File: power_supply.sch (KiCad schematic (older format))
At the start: 62 parts, among them J1 12v, 0.5A nominal, 5A Surge, J2 5V 25W, J3 Fan, J4 Program, J5 Shutdown, J6 12V 5V, J7 Serial Debug, J8 REMOVE to PRGM, J9 Main PWR SW, M1 U3V70F5, M2 XL4015, M3 U1V11F5, Q1 BSS806, Q2 BSS806, Q3 SI2369BDS, Q4 BSS806, Q5 IRF9540NPBF, U1 ALD910027, U2 MCP9700A, U3 BTS443P, U4 PIC16F1709, U5 MCP111-195

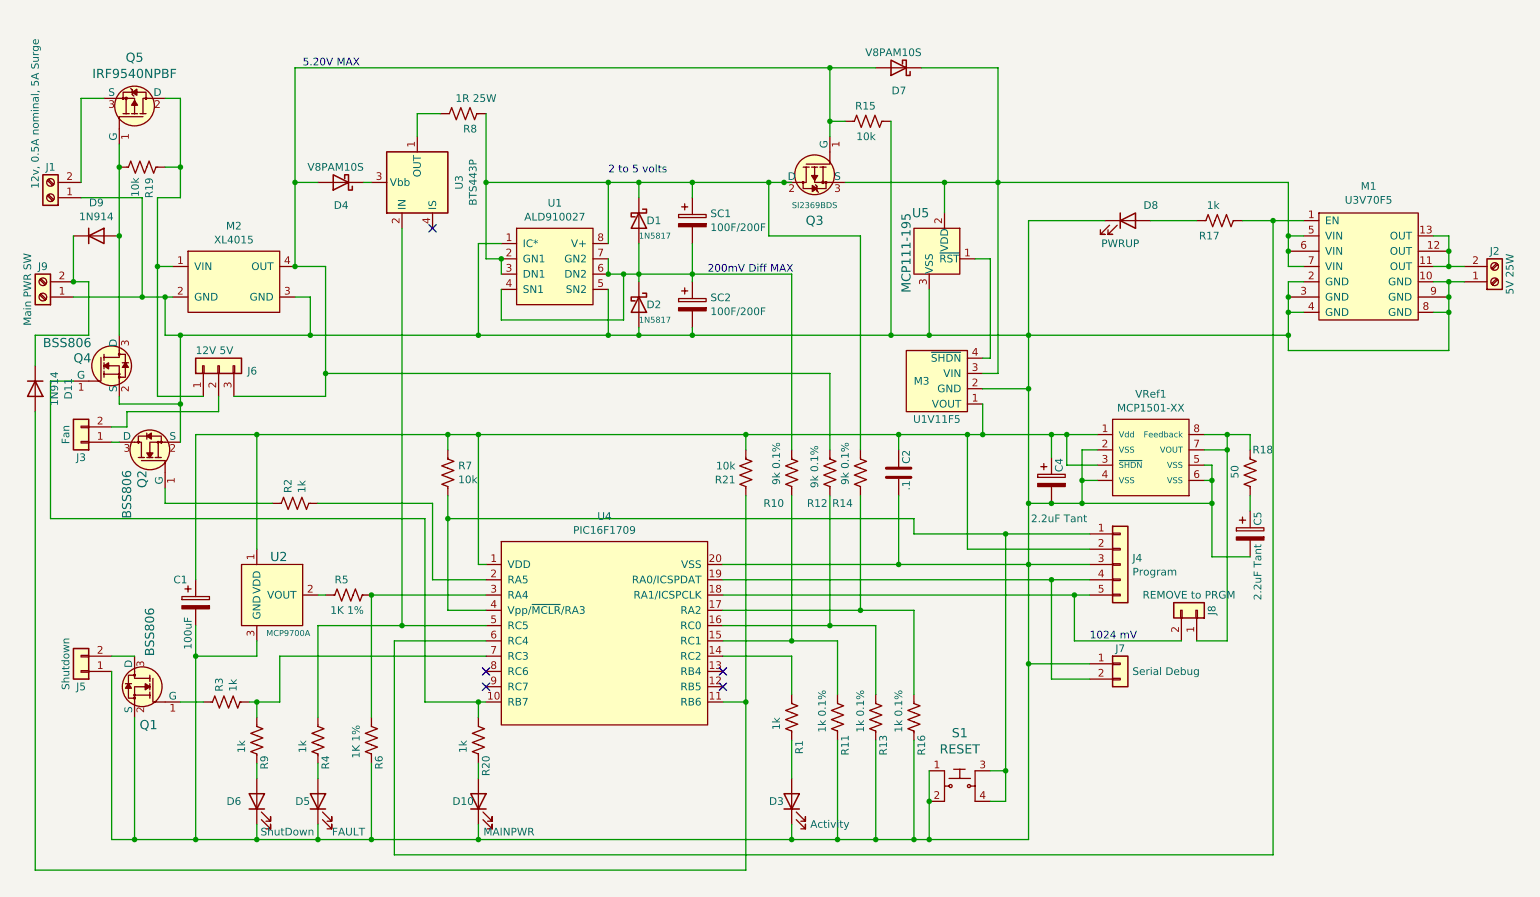
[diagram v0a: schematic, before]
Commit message: Version 0.35 includes updates for new parts and field updates for PCB
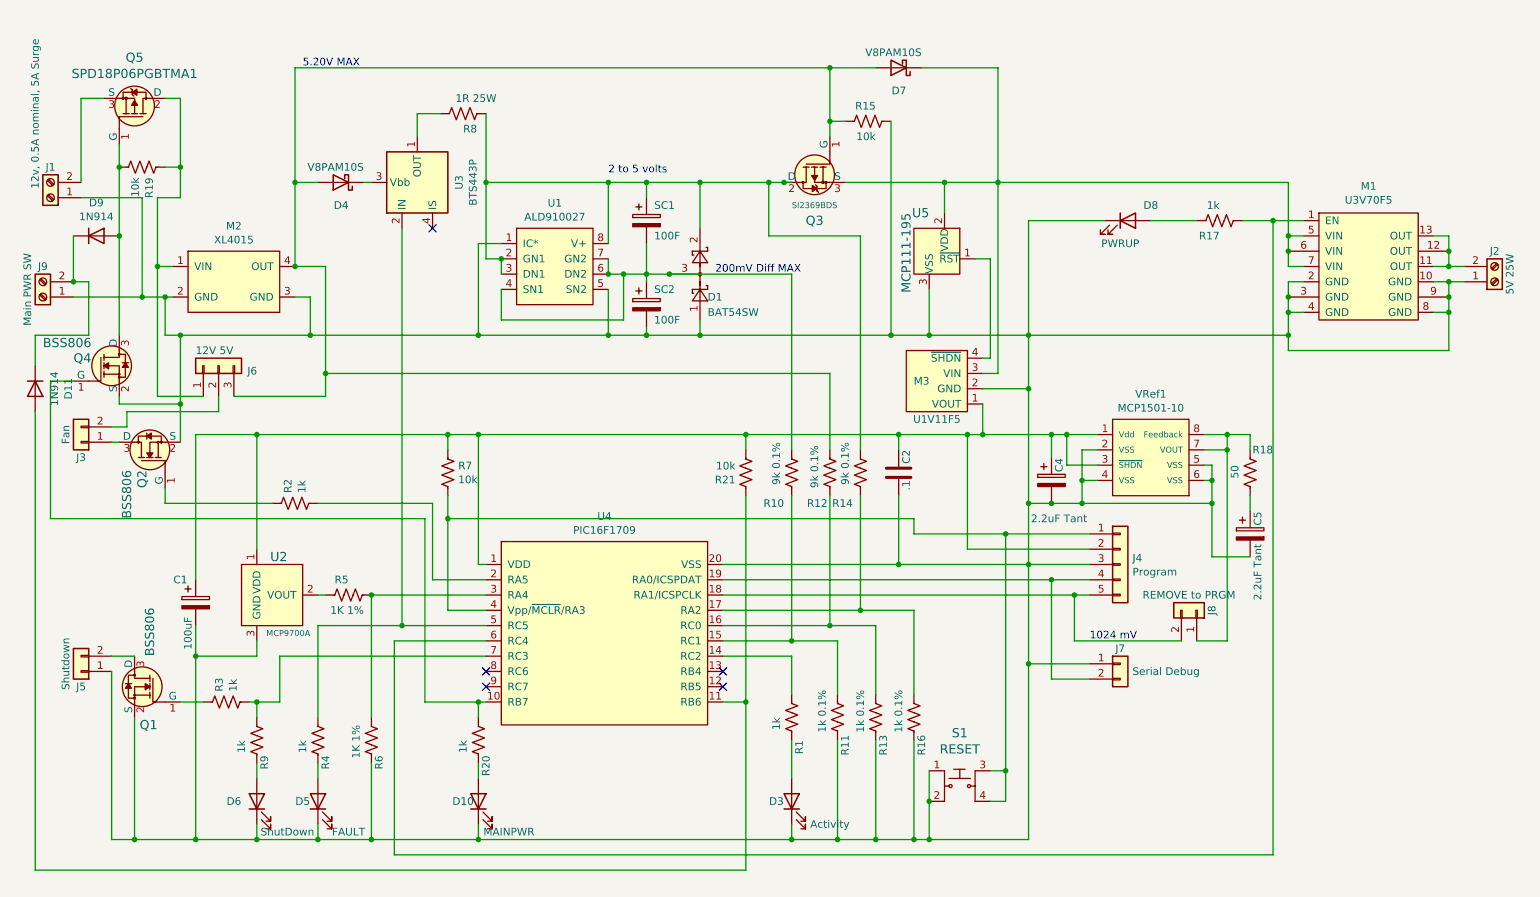
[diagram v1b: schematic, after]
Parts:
- removed D1, D2: 1N5817, Diode_THT:D_DO-41_SOD81_P10.16mm_Horizontal, symbol Diode:1N5817
- added D1: BAT54SW, Package_TO_SOT_SMD:SOT-323_SC-70, symbol Diode:BAT54SW
- C1: footprint (none) -> Capacitor_SMD:CP_Elec_6.3x5.2
- C4, C5: footprint (none) -> Capacitor_Tantalum_SMD:CP_EIA-3216-18_Kemet-A; Part# (none) -> 80-T491A225K010; Vendor (none) -> Mouser
- D4, D7: Part# (none) -> 78-V8PAM10SHM3/H; Vendor (none) -> Mouser
- M2: footprint (none) -> Footprint_Library:XL4015
- M3: footprint (none) -> Pololu:U1V11Fx
- Q1: Category Discrete Semiconductor Products -> (none); DK_Datasheet_Link https://www.onsemi.com/pub/Collateral/BSS138-D.PDF -> (none); DK_Detail_Page /product-detail/en/on-semiconductor/BSS138/BSS138CT-ND/2442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 -> (none); Description MOSFET N-CH 50V 220MA SOT-23 -> (none); Digi-Key_PN BSS138CT-ND -> (none); Family Transistors - FETs, MOSFETs - Single -> (none); MPN BSS138 -> (none); Manufacturer ON Semiconductor -> (none); Part# (none) -> 726-BSS806NEH6327XTS; Status Active -> (none); Vendor (none) -> Mouser
- Q2, Q4: Part# (none) -> 726-BSS806NEH6327XTS; Vendor (none) -> Mouser
- Q5: value IRF9540NPBF -> SPD18P06PGBTMA1; footprint digikey-footprints:TO-220-3 -> Package_TO_SOT_SMD:TO-252-3_TabPin2
- SC1, SC2: value 100F/200F -> 100F
- U1: Part# (none) -> 585-ALD910027SAL; Vendor (none) -> Mouser
- U2: Category Sensors, Transducers -> (none); DK_Datasheet_Link http://www.microchip.com/mymicrochip/filehandler.aspx?ddocn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 -> (none); DK_Detail_Page /product-detail/en/microchip-technology/MCP9700A-E-TO/MCP97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 -> (none); Description SENSOR ANALOG -40C-125C TO92-3 -> (none); Digi-Key_PN MCP9700A-E/TO-ND -> (none); Family Temperature Sensors - Analog and Digital Output -> (none); MPN MCP9700A-E/TO -> (none); Manufacturer Microchip Technology -> (none); Part# (none) -> 579-MCP9700A-E/TO; Status Active -> (none); Vendor (none) -> Mouser
- U4: footprint (none) -> Package_SO:SOIC-20W_7.5x12.8mm_P1.27mm; Part# (none) -> 579-PIC16F1709T-I/SO; Vendor (none) -> Mouser
- VRef1: value MCP1501-XX -> MCP1501-10; footprint (none) -> digikey-footprints:SOT-23-6; Part# (none) -> 579-MCP1501T-10E/CHY
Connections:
- net at C1.2, C2.1, C4.2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: now also D1.1
- net at Q3.2 (D), R14.1, R8.2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: now also D1.2
- net at R10.1, SC1.1, SC2.2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: now also D1.3
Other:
- moved on the sheet: SC1, SC2

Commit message: Version 0.36 circuit part changes, completed initial parts information and BOM
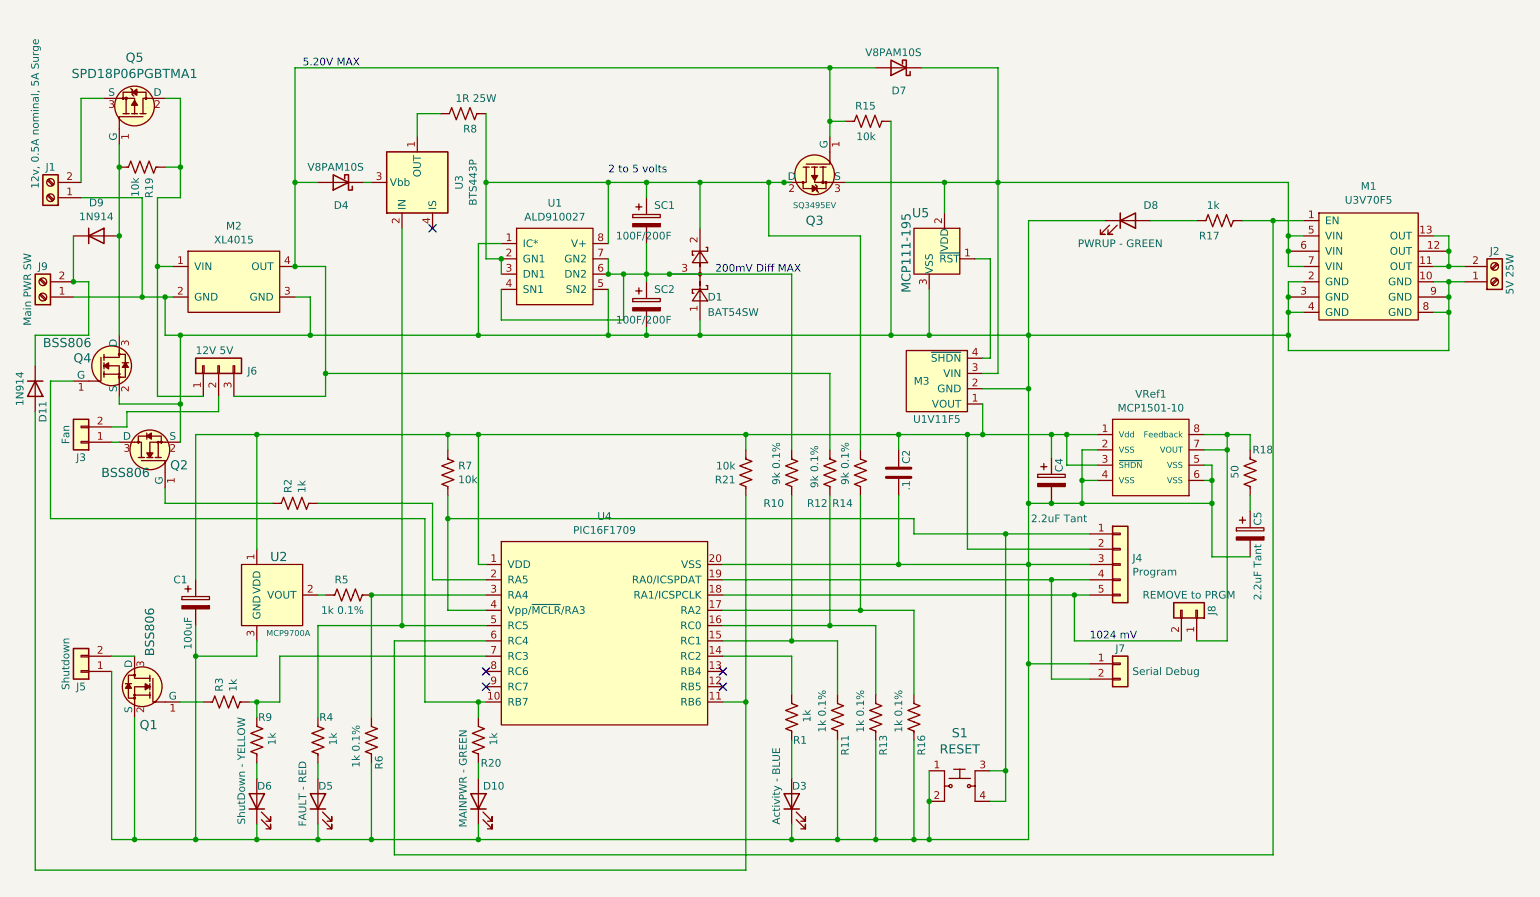
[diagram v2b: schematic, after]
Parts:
- C1: Part# (none) -> 661-EMVY160ADA101MF5; Vendor (none) -> Mouser
- C2: Part# (none) -> 77-VJ1206Y104MXJPBC; Vendor (none) -> Mouser
- D10: value MAINPWR -> MAINPWR - GREEN; Part# (none) -> 645-598-8270-107F; Vendor (none) -> Mouser
- D11, D9: footprint Diode_THT:D_DO-35_SOD27_P7.62mm_Horizontal -> Diode_SMD:D_SOD-123F; Part# (none) -> 821-1N914BWRHG; Vendor (none) -> Mouser
- D3: value Activity -> Activity - BLUE; Part# (none) -> 645-598-8291-107F; Vendor (none) -> Mouser
- D5: value FAULT -> FAULT - RED; Part# (none) -> 645-598-8220-107F; Vendor (none) -> Mouser
- D6: value ShutDown -> ShutDown - YELLOW; Part# (none) -> 645-598-8240-107F; Vendor (none) -> Mouser
- D8: value PWRUP -> PWRUP - GREEN; Part# (none) -> 645-598-8270-107F; Vendor (none) -> Mouser
- J1, J2, J9: Part# (none) -> https://www.amazon.com/Pieces-Pinch-Mount-Terminal-Connecto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; Vendor (none) -> Amazon
- J3, J4, J5, J7, J8: Part# (none) -> https://www.amazon.com/Header-Lystaii-Pin-Connector-Electro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; Vendor (none) -> Amazon
- J6: footprint (none) -> Connector_PinHeader_2.54mm:PinHeader_1x03_P2.54mm_Vertical; Part# (none) -> https://www.amazon.com/Header-Lystaii-Pin-Connector-Electro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; Vendor (none) -> Amazon
- M1: Part# (none) -> 2891; Vendor (none) -> Pololu
- M2: Part# (none) -> https://www.amazon.com/Adjustable-Converter-1-25-36v-Effici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; Vendor (none) -> Amazon
- M3: Part# (none) -> 2562; Vendor (none) -> Pololu
- Q3: value SI2369BDS -> SQ3495EV; footprint digikey-footprints:TO-220-3 -> digikey-footprints:SOT-23-6; Part# (none) -> 78-SQ3495EV-T1_GE3; Vendor (none) -> Mouser
- Q5: Part# (none) -> 726-SPD18P06P; Vendor (none) -> Mouser
- R1, R17, R2, R20, R3, R4, R9: Part# (none) -> 603-RT1206FRD071KL; Vendor (none) -> Mouser
- R10, R12, R14: Part# (none) -> 603-RT1206BRD079KL; Vendor (none) -> Mouser
- R11, R13, R16: Part# (none) -> 603-RT1206BRD071KL; Vendor (none) -> Mouser
- R15, R19, R21, R7: Part# (none) -> 603-RT1206FRD0710KL; Vendor (none) -> Mouser
- R18: Part# (none) -> 660-RN732BTTD50R0B25; Vendor (none) -> Mouser
- R5, R6: value 1K 1% -> 1k 0.1%; Part# (none) -> 603-RT1206BRD071KL; Vendor (none) -> Mouser
- R8: footprint Resistor_SMD:R_1206_3216Metric -> Connector_Wire:SolderWire-0.25sqmm_1x02_P4.5mm_D0.65mm_OD2mm; Part# (none) -> 71-RH0251R000FE02; Vendor (none) -> Mouser
- S1: footprint digikey-footprints:Switch_Tactile_THT_6x6mm -> digikey-footprints:Switch_Tactile_SMD_6x6mm; Part# (none) -> 667-EVQ-7Q201W; Vendor (none) -> Mouser
- SC1, SC2: value 100F -> 100F/200F; Part# (none) -> 581-SCCW45B107SSB / 581-SCCW45B207SSB; Vendor (none) -> Mouser
- U3: Part# (none) -> 726-BTS443P; Vendor (none) -> Mouser
- U5: Part# (none) -> 579-MCP111T-195I/TT; Vendor (none) -> Mouser
- VRef1: Vendor (none) -> Mouser

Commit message: Version 1.0 includes fixes/changes and FRAM support
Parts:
- removed J3: Fan, Connector_PinHeader_2.54mm:PinHeader_1x02_P2.54mm_Vertical, symbol Connector_Generic:Conn_01x02
- removed J9: Main PWR SW, Connectors:Screw_Terminal_2Pin, symbol Connector:Screw_Terminal_01x02
- removed Q3: SQ3495EV, digikey-footprints:SOT-23-6, symbol dk_Transistors-FETs-MOSFETs-Single:IRF9540NPBF
- removed VRef1: MCP1501-10, digikey-footprints:SOT-23-6, symbol Geekgineering:MCP1501-XX
- added C5, C6: 1uF, Capacitor_SMD:C_1206_3216Metric_Pad1.33x1.80mm_HandSolder, symbol Device:CP
- added J2: Power Switch, Connector_JST:JST_XH_B5B-XH-A_1x05_P2.50mm_Vertical, symbol Connector_Generic:Conn_01x05
- added J9: FRAM I2C, Connector_JST:JST_XH_B3B-XH-A_1x03_P2.50mm_Vertical, symbol Connector_Generic:Conn_01x03
- added Q4: BSS806, digikey-footprints:SOT-23-3, symbol dk_Transistors-FETs-MOSFETs-Single:BSS138
- added Q6: SQ3495-EV, digikey-footprints:SOT-23-6, symbol Geekgineering:SQ3495-EV
- added R23, R24: 10k, Resistor_SMD:R_1206_3216Metric, symbol Device:R_US
- added R5: 1k, Resistor_SMD:R_1206_3216Metric, symbol Device:R_US
- added U6: MB85RC1MT, Package_SO:SOIC-8_3.9x4.9mm_P1.27mm, symbol Geekgineering:MR44V100AMAZAATL
- added U7: MCP1700-3302E_SOT23, Package_TO_SOT_SMD:SOT-23, symbol Regulator_Linear:MCP1700-3302E_SOT23
- added VRef1: MCP1501-6Pin, digikey-footprints:SOT-23-6, symbol Geekgineering:MCP1501-6Pin
- C2: footprint Capacitor_SMD:C_1206_3216Metric_Pad1.42x1.75mm_HandSolder -> Capacitor_SMD:C_1206_3216Metric_Pad1.33x1.80mm_HandSolder
- D10: renamed from D8; value PWRUP - GREEN -> PWRUP
- D3: renamed from D6; value ShutDown - YELLOW -> ShutDown
- D4: renamed from D5; value FAULT - RED -> FAULT
- D5: renamed from D4; footprint Diode_THT:D_DO-41_SOD81_P10.16mm_Horizontal -> Footprint_Library:DO-221BC
- D6: renamed from D10; value MAINPWR - GREEN -> MAINPWR
- D8: renamed from D3; value Activity - BLUE -> Activity
- D9: renamed from D7; footprint Diode_THT:D_DO-41_SOD81_P10.16mm_Horizontal -> Footprint_Library:DO-221BC
- M3: renamed from M1; footprint Pololu Regulators:U3V70F5 -> Pololu:U3V70F5
- R10: renamed from R8; footprint Connector_Wire:SolderWire-0.25sqmm_1x02_P4.5mm_D0.65mm_OD2mm -> Connector_Wire:SolderWire-0.5sqmm_1x02_P4.6mm_D0.9mm_OD2.1mm
- SC1, SC2: footprint SuperCaps:SCC-30mm -> SuperCaps:SCC-22-30mm
- U1: renamed from U2; footprint digikey-footprints:TO-92-3 -> digikey-footprints:SOT-23-3; Part# 579-MCP9700A-E/TO -> 579-MCP9700AT-E/TT
- renumbered C4 to C3, C5 to C4, D11 to D1, D9 to D2, D1 to D7, J5 to J3, J6 to J4, J4 to J5, J7 to J6, J8 to J7, J2 to J8, M2 to M1, M3 to M2, Q4 to Q1, Q5 to Q3, Q1 to Q5, R19 to R1, R20 to R11, R21 to R12, R10 to R13, R1 to R14, R12 to R15, R11 to R16, R14 to R17, R15 to R18, R13 to R19, R3 to R2, R16 to R20, R17 to R21, R18 to R22, R9 to R3, R2 to R4, R4 to R6, R5 to R7, R6 to R8, R7 to R9, U3 to U2, U1 to U3
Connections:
- net at M3.1 (EN), R21.1, U4.6 (RC4): now also R5.1
- net at C1.2, C2.1, C3.2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: now also C5.2, C6.2, J2.1 (Pin_1), J9.1 (Pin_1), Q4.2 (S), U6.4 (VSS), U7.1 (GND), VRef1.2 (VSS), VRef1.3 (VSS), VRef1.5 (VSS)
- net at J8.2 (Pin_2), M3.11 (OUT), M3.12 (OUT)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: now also C6.1, J2.4 (Pin_4), U7.3 (VI)
- net at D9.1 (K), M2.3 (VIN), M3.5 (VIN)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: now also Q6.4 (S)
- net at D7.2, R10.2, R17.1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: now also Q6.1 (D), Q6.2 (D), Q6.5 (D), Q6.6 (D)
- net at C1.1, C2.2, C3.1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: now also VRef1.4 (~SHDN), VRef1.6 (Vdd)
- net at D5.2 (A), D9.2 (A), J4.3 (Pin_3)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: now also Q6.3 (G)
- net at Q2.3 (D): now also J4.2 (Pin_2)
- net at J7.1 (Pin_1), R22.1: now also VRef1.1 (VOUT)
- net at J4.1 (Pin_1), M1.1 (VIN), Q3.2 (D)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: now also J2.3 (Pin_3)
- net at D1.1 (K), D2.1 (K): now also J2.2 (Pin_2)
- new net: Q4.1 (G), R5.2
- new net: J2.5 (Pin_5), Q4.3 (D)
- new net: J9.2 (Pin_2), R24.2, U6.5 (SDA)
- new net: J9.3 (Pin_3), R23.2, U6.6 (SCL)
- new net: C5.1, R23.1, R24.1, U6.8 (VCC), U7.2 (VO)
- no-connect marks 5 -> 9
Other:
- moved on the sheet: D1, Q2
